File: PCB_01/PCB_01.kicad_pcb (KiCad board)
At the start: 2 copper layers, 40 parts, among them J1 TOUCH_E0, J2 UIM2040PM_Power, J4 UIM2040PM_Signal, J5 BNO055 Adafruit, J6 RAPC712TRP22X, J8 UJ20-C-H-G-MSMT-R-4C-P16-TR, Q1 FS8205A, U1 TP4056, U2 MT3608, U3 MPR121QR2, U4 DFR0299, U5 DW01S

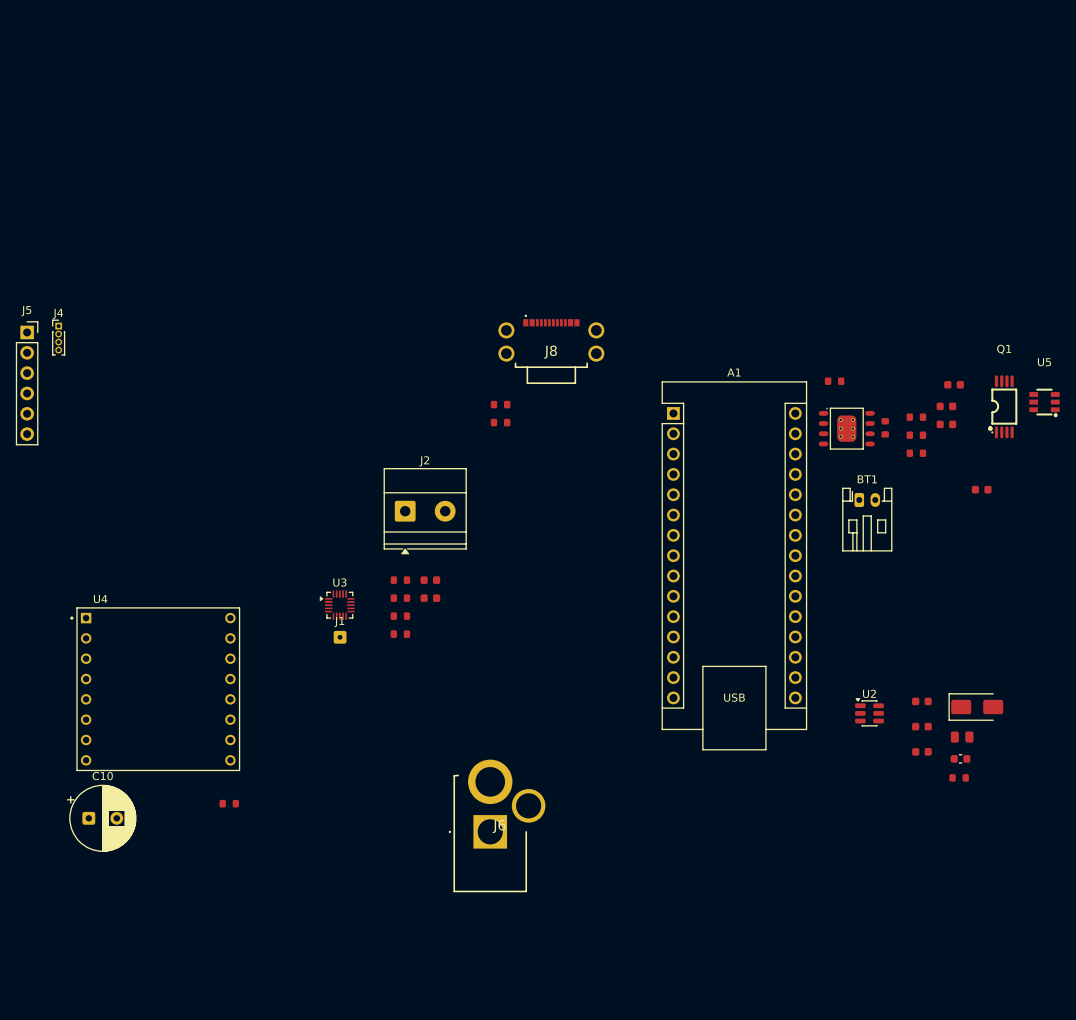
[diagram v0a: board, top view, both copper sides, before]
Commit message: Update KiCad PCB layout and schematic, add Molex connector footprints and STEP models, and generate production outputs (BOM, interactive BOM, positions, and fabrication zip files)
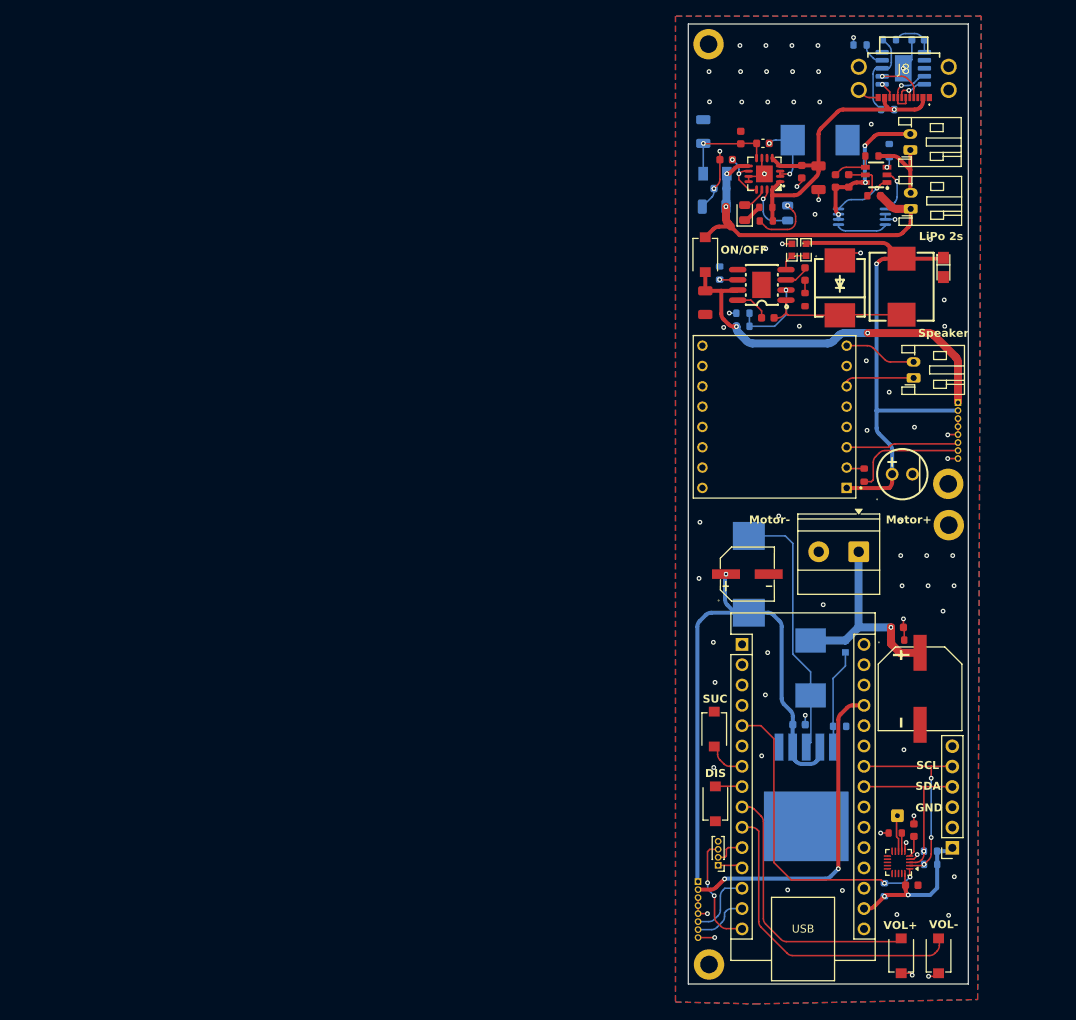
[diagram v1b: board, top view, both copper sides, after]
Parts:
- removed C10: C_Polarized, Capacitor_THT:CP_Radial_D8.0mm_P3.50mm
- added BT2: Battery_Cell LiPo, Connector_JST:JST_PH_S2B-PH-K_1x02_P2.00mm_Horizontal, F.Cu at (130.4, 70.4)
- added C12: 10uF, PCM_JLCPCB:C_1206, F.Cu at (104.8, 89.5)
- added C13: 100nF, PCM_JLCPCB:C_0603, F.Cu at (109.2, 68.9)
- added C14: 100nF, PCM_JLCPCB:C_0603, F.Cu at (112.6, 91.4)
- added C15: 100nF, PCM_JLCPCB:C_0603, B.Cu at (106.7, 75.2)
- added C16: CA45-A-6.3V-22UF-K, EasyEDA:CASE-A_3216, F.Cu at (134.6, 85.1)
- added C17: 100nF, PCM_JLCPCB:C_0603, F.Cu at (107.4, 71.6)
- added C18: 150pF, PCM_JLCPCB:C_0603, F.Cu at (117.3, 85.9)
- added C19: 100nF, PCM_JLCPCB:C_0603, F.Cu at (128.8, 130.1)
- added C20: 100nF, PCM_JLCPCB:C_0603, F.Cu at (122.7, 74.3)
- added C21: 100nF, PCM_JLCPCB:C_0603, F.Cu at (121.1, 74.3)
- added C22: KMG-10V470-6.3*11, EasyEDA:CAP-TH_BD6.3-P2.50-D1.0-FD, F.Cu at (129.4, 110.9)
- added C7: 100nF, PCM_JLCPCB:C_0603, F.Cu at (116.9, 73.1)
- added D1: B540C-13-F, EasyEDA:SMC_L7.1-W6.2-LS8.1-RD, B.Cu at (119.2, 69.2)
- added D2: B540C-13-F, EasyEDA:SMC_L7.1-W6.2-LS8.1-RD, B.Cu at (118.0, 135.2)
- added D4: LED, LED_SMD:LED_0805_2012Metric, F.Cu at (109.7, 78.2)
- added D5: LED, LED_SMD:LED_0805_2012Metric, B.Cu at (115.1, 78.3)
- added H1: MountingHole_Pad, MountingHole:MountingHole_2.2mm_M2_DIN965_Pad, F.Cu at (105.2, 57.2)
- added H2: MountingHole_Pad, MountingHole:MountingHole_2.2mm_M2_DIN965_Pad, F.Cu at (135.2, 117.3)
- added H3: MountingHole_Pad, MountingHole:MountingHole_2.2mm_M2_DIN965_Pad, F.Cu at (135.2, 112.2)
- added H4: MountingHole_Pad, MountingHole:MountingHole_2.2mm_M2_DIN965_Pad, F.Cu at (105.3, 172.2)
- added J3: PinHeader_1x08, Connector_PinHeader_1.00mm:PinHeader_1x08_P1.00mm_Vertical, B.Cu at (136.4, 102.0)
- added J7: Speaker, Connector_JST:JST_PH_S2B-PH-K_1x02_P2.00mm_Horizontal, F.Cu at (130.8, 98.9)
- added L2: CXP0850-150M-AG, EasyEDA:IND-SMD_L8.5-W8.0_PCC-M0854M, F.Cu at (129.3, 87.5)
- added R12: 1kΩ, PCM_JLCPCB:R_0603, F.Cu at (112.4, 77.6)
- added R13: 1kΩ, PCM_JLCPCB:R_0603, F.Cu at (112.4, 79.3)
- added R17: HOJLR1206-1W-100MR-1%, EasyEDA:RES-SMD_L3.2-W1.6_SY1206, B.Cu at (106.0, 73.4)
- added R18: RCA0340K2FLF, EasyEDA:R0603, F.Cu at (115.6, 82.9)
- added R19: 100kΩ, PCM_JLCPCB:R_0603, F.Cu at (117.3, 89.1)
- added R20: 100kΩ, PCM_JLCPCB:R_0603, B.Cu at (109.5, 92.5)
- added R21: 330Ω, PCM_JLCPCB:R_0603, F.Cu at (125.9, 76.1)
- added R22: 330Ω, PCM_JLCPCB:R_0603, F.Cu at (125.6, 71.2)
- added R23: 2kΩ, PCM_JLCPCB:R_0603, B.Cu at (127.8, 70.5)
- added SW1: TS-1088-AR02016, EasyEDA:SW-SMD_L3.9-W3.0-P4.45, F.Cu at (105.9, 142.8)
- added SW2: TS-1088-AR02016, EasyEDA:SW-SMD_L3.9-W3.0-P4.45, F.Cu at (106.1, 152.2)
- added SW3: TS-1088-AR02016, EasyEDA:SW-SMD_L3.9-W3.0-P4.45, F.Cu at (129.3, 171.1)
- added SW4: TS-1088-AR02016, EasyEDA:SW-SMD_L3.9-W3.0-P4.45, F.Cu at (134.0, 171.1)
- added SW5: TS-1088-AR02016, EasyEDA:SW-SMD_L3.9-W3.0-P4.45, F.Cu at (104.8, 83.5)
- added U7: MP1584EN, EasyEDA:SOIC-8_L4.9-W3.9-P1.27-LS6.0-BL-EP3.3, F.Cu at (111.9, 87.3)
- added U8: HY2120-LB, EasyEDA:SOT-23-6_L2.9-W1.6-P0.95-LS2.8-BR, F.Cu at (126.2, 73.5)
- added U9: TP5100_C379389, EasyEDA:TQFN-16_L4.0-W4.0-P0.65-BL-EP, F.Cu at (112.2, 73.4)
- C1: value 100nF -> 1uF; moved to B.Cu
- C11, C6: footprint PCM_JLCPCB:C_0603 -> PCM_JLCPCB:C_1206; moved to B.Cu
- C2: value 100nF -> 10uF; footprint PCM_JLCPCB:C_0603 -> PCM_JLCPCB:C_1206
- C3: value 10uF -> RVT1H470M0607 47UF 50V; footprint PCM_JLCPCB:C_0603 -> EasyEDA:CAP-SMD_BD6.3-L6.6-W6.6-LS7.2-FD
- C4: value 10uF -> 1uF; moved to B.Cu
- C5: value 10uF -> MVK 50V220; footprint PCM_JLCPCB:C_0603 -> EasyEDA:CAP-SMD_BD10.0-L10.3-W10.3-FD
- D3: value SS34 -> B540C-13-F; footprint PCM_JLCPCB:D_SMA -> EasyEDA:SMC_L7.1-W6.2-LS8.1-RD
- J1, R10, R11, R3, R9: moved to B.Cu
- J6: value RAPC712TRP22X -> Conn_01x08_Socket; footprint RAPC712TRP22X:RAPC712TRP22X -> Connector_PinSocket_1.00mm:PinSocket_1x08_P1.00mm_Vertical; moved to B.Cu
- Q1: value FS8205A -> 8205A; footprint FS8205A:TSSOP-8_L4.4-W3.0-P0.65-LS6.4-BL-2 -> EasyEDA:TSSOP-8_L4.4-W3.0-P0.65-LS6.4-BL; moved to B.Cu
- R1: value 1.2kΩ -> 24kΩ; moved to B.Cu
- R15: value 5.1kΩ -> 100kΩ; moved to B.Cu
- R16: value 5.1kΩ -> 0603WAF2103T5E; footprint PCM_JLCPCB:R_0603 -> EasyEDA:R0603
- R2: value 1kΩ -> 10kΩ; moved to B.Cu
- R4: value 16kΩ -> 1kΩ; footprint PCM_JLCPCB:R_0805 -> PCM_JLCPCB:R_0603; moved to B.Cu
- R5: value 100Ω -> RCT0318K2FLF; footprint PCM_JLCPCB:R_0603 -> EasyEDA:R0603; moved to B.Cu
- R7: value 2.2kΩ -> 100kΩ; moved to B.Cu
- U1: value TP4056 -> CH224K; footprint PCM_JLCPCB:ESOP-8_L4.9-W3.9-P1.27-LS6.0-BL-EP -> Package_SO:SSOP-10-1EP_3.9x4.9mm_P1mm_EP2.1x3.3mm; moved to B.Cu
- U2: value MT3608 -> XL6009; footprint Package_TO_SOT_SMD:SOT-23-6 -> EasyEDA:TO-263-5_L10.2-W8.6-P1.70-LS14.4-TL; moved to B.Cu
- U5: value DW01S -> CKST1004-33UH/M; footprint DW01S:SOT-23-6_L2.9-W1.6-P0.95-LS2.8-BR -> EasyEDA:IND-SMD_L11.6-W10.1; moved to B.Cu
- moved J5 132.4 mm to (135.7, 157.7), turned to 180 degrees
- moved J4 106.5 mm to (106.4, 159.8), turned to 180 degrees
- moved R14 89.4 mm to (124.7, 111.1), turned to -90 degrees
- moved U4 84.2 mm to (113.5, 103.8), turned to 180 degrees
- moved C6 82.2 mm to (104.5, 68.1), turned to 90 degrees
- moved L1 80.8 mm to (112.0, 69.6), turned to 180 degrees
- moved U3 76.9 mm to (129.0, 159.5), turned to 180 degrees
- moved R9 73.4 mm to (132.9, 158.1), turned to 180 degrees
- moved R10 73.2 mm to (133.0, 159.7), turned to 180 degrees
- moved J1 73.2 mm to (128.8, 153.6)
- moved C8 71.2 mm to (130.6, 162.3)
- moved R8 69.5 mm to (128.5, 155.8), turned to 180 degrees
- moved R11 68.4 mm to (127.2, 162.9), turned to 90 degrees
- moved C9 67.0 mm to (130.9, 155.4), turned to 90 degrees
- moved R7 64.1 mm to (109.5, 90.8)
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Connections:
- A1 pad 11: unconnected-(A1-D8-Pad11) -> UIM_DIR
- A1 pad 12: unconnected-(A1-D9-Pad12) -> UIM_STEP
- A1 pad 15: unconnected-(A1-D12-Pad15) -> UIM_ENA
- A1 pad 29: USB- -> P-
- A1 pad 4: USB- -> P-
- BT1 pad 2: B- -> BM
- C1 pad 1: USB+ -> P-
- C1 pad 2: USB- -> Net-(U1-VDD)
- C11 pad 2: USB- -> P-
- C2 pad 1: Net-(U5-VDD) -> Vin
- C2 pad 2: B- -> P-
- C3 pad 1: USB+ -> SW+
- C3 pad 2: USB- -> P-
- C4 pad 1: B+ -> SW+
- C4 pad 2: USB- -> P-
- C5 pad 1: +5V -> +24V
- C5 pad 2: USB- -> P-
- C6 pad 1: +5V -> Net-(U9-VS)
- C6 pad 2: USB- -> P-
- C8 pad 2: USB- -> P-
- C9 pad 2: USB- -> P-
- D3 pad 1: +5V -> Net-(D3-K)
- D3 pad 2: Net-(U2-SW) -> P-
- J2 pad 1: Net-(J2-Pin_1) -> +24V
- J2 pad 2: Net-(J2-Pin_2) -> P-
- J4 pad 4: USB- -> P-
- J5 pad 3: USB- -> P-
- J6 pad 1: Net-(J2-Pin_1) -> SW+
- J6 pad 2: unconnected-(J6-Pad2) -> +5V
- J6 pad 3: Net-(J2-Pin_2) -> P-
- J8 pad A1: USB- -> P-
- J8 pad A12: USB- -> P-
- J8 pad A4: USB+ -> Vin
- J8 pad A5: Net-(J8-CC1) -> USB_CC1
- J8 pad A6: unconnected-(J8-DP1-PadA6) -> USB_DP
- J8 pad A7: unconnected-(J8-DN1-PadA7) -> USB_DN
- J8 pad A9: USB+ -> Vin
- J8 pad B5: Net-(J8-CC2) -> USB_CC2
- J8 pad B6: unconnected-(J8-DP2-PadB6) -> USB_DP
- J8 pad B7: unconnected-(J8-DN2-PadB7) -> USB_DN
- J8 pad MH1: USB- -> P-
- J8 pad MH2: USB- -> P-
- J8 pad MH3: USB- -> P-
- J8 pad MH4: USB- -> P-
- L1 pad 1: B+ -> Net-(D1-K)
- L1 pad 2: Net-(U2-SW) -> Net-(U9-VS)
- Q1 pad 4: Net-(Q1-G1) -> OD
- Q1 pad 5: Net-(Q1-G2) -> OC
- Q1 pad 6: USB- -> P-
- Q1 pad 7: USB- -> P-
- R1 pad 1: Net-(U1-PROG) -> Net-(U1-CFG1)
- R1 pad 2: USB- -> P-
- R15 pad 1: Net-(J8-CC2) -> P-
- R15 pad 2: USB- -> Net-(U7-FREQ)
- R16 pad 1: USB- -> +5V
- R16 pad 2: Net-(J8-CC1) -> Net-(U7-FB)
- R2 pad 1: Net-(D2-K) -> Vin
- R2 pad 2: Net-(U1-CHRG#) -> Net-(U1-VBUS)
- R3 pad 1: Net-(U5-CSI) -> Net-(U1-VBUS)
- R3 pad 2: USB- -> Net-(U1-VDD)
- R4 pad 1: +5V -> P-
- R5 pad 1: Net-(U5-VDD) -> +24V
- R5 pad 2: B+ -> Net-(U2-FB)
- R6 pad 1: Net-(D1-K) -> P-
- R6 pad 2: Net-(U1-STDBY#) -> +24V
- R7 pad 1: Net-(U2-FB) -> P-
- R7 pad 2: USB- -> EN
- R8 pad 2: USB- -> P-
- U1 pad 1: USB- -> Net-(U1-VDD)
- U1 pad 2: Net-(U1-PROG) -> unconnected-(U1-CFG2-Pad2)
- U1 pad 3: USB- -> unconnected-(U1-CFG3-Pad3)
- U1 pad 4: USB+ -> USB_DP
- U1 pad 5: unconnected-(U1-BAT-Pad5) -> USB_DN
- U1 pad 6: Net-(U1-STDBY#) -> USB_CC2
- U1 pad 7: Net-(U1-CHRG#) -> USB_CC1
- U1 pad 8: USB+ -> Net-(U1-VBUS)
- U1 pad 9: unconnected-(U1-EP-Pad9)_1 -> Net-(U1-CFG1)
- U2 pad 1: Net-(U2-SW) -> P-
- U2 pad 2: USB- -> SW+
- U2 pad 3: Net-(U2-FB) -> Net-(D2-A)
- U2 pad 4: B+ -> SW+
- U2 pad 5: B+ -> Net-(U2-FB)
- U2 pad 6: unconnected-(U2-NC-Pad6) -> P-
- U3 pad 4: USB- -> P-
- U3 pad 6: USB- -> P-
- U4 pad 10: USB- -> P-
- U4 pad 16: DFR_BUSY -> unconnected-(U4-BUSY-Pad16)
- U4 pad 7: USB- -> P-
- U5 pad 1: Net-(Q1-G1) -> SW+
- U5 pad 2: Net-(U5-CSI) -> Net-(D2-A)
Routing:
- net SW+: track 0.00 -> 121.1 mm, vias 0 -> 3
- net +5V: track 0.00 -> 107.0 mm, vias 0 -> 3
- net P-: track 0.00 -> 50.9 mm, vias 0 -> 73
- net B+: track 0.00 -> 43.4 mm, vias 0 -> 2
- net Vin: track 0.00 -> 41.2 mm, vias 0 -> 1
- net /VOLDOWN: track 0.00 -> 39.6 mm
- net MPR_IRQ: track 0.00 -> 39.6 mm, vias 0 -> 2
- net /VOLUP: track 0.00 -> 34.9 mm
- net Net-(D2-A): track 0.00 -> 32.5 mm
- net +24V: track 0.00 -> 26.3 mm, vias 0 -> 1
- net I2C_SCL: track 0.00 -> 25.5 mm, vias 0 -> 3
- net ARD_RX: track 0.00 -> 22.7 mm
- net I2C_SDA: track 0.00 -> 21.9 mm, vias 0 -> 1
- net ARD_TX: track 0.00 -> 21.7 mm
- net +3.3V: track 0.00 -> 19.6 mm, vias 0 -> 2
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- added copper zone on B.Cu, net P-
- added copper zone on F.Cu, net P-
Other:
- board outline added: 35 x 120 mm
- board text added: "DIS"
- board text added: "GND"
- board text added: "LiPo 2s"
- board text added: "Motor+"
- board text added: "Motor-"
- board text added: "ON/OFF"
- board text added: "SCL"
- board text added: "SDA"
- board text added: "SUC"
- board text added: "Speaker"
- board text added: "USB"
- board text added: "VOL+"
- board text added: "VOL-"
